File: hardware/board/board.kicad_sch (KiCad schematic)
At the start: 37 parts, among them J101 CM4_UART, J102 CM4_DEBUG, J103 MCU_DEBUG, J104 MCU_UART, J105 Conn_01x01, J106 CM4_STATUS, J107 Barrel_Jack, J108 Conn_01x01, J109 Conn_01x01, J110 Conn_01x01, J111 Conn_01x01, U101 Oled, U104 74LVC1G07SE-7, U105 NCP1117-3.3_SOT223

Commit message: footprints
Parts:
- D101, D102: footprint LED_SMD:LED_0603_1608Metric -> LED_SMD:LED_0805_2012Metric
- J104, J106: footprint (none) -> Connector_PinSocket_2.54mm:PinSocket_1x03_P2.54mm_Vertical
- J105: value Conn_01x01 -> MCU_RUN; footprint (none) -> Connector_PinSocket_2.54mm:PinSocket_1x01_P2.54mm_Vertical
- J107: value Barrel_Jack -> Barrel_5V; footprint (none) -> ledaw:DC-005-5A-2.0
- J108: value Conn_01x01 -> TP_3V3; footprint (none) -> Connector_PinSocket_2.54mm:PinSocket_1x01_P2.54mm_Vertical
- J109: value Conn_01x01 -> TP_1V8; footprint (none) -> Connector_PinSocket_2.54mm:PinSocket_1x01_P2.54mm_Vertical
- J110: value Conn_01x01 -> TP_5V; footprint (none) -> Connector_PinSocket_2.54mm:PinSocket_1x01_P2.54mm_Vertical
- J111: value Conn_01x01 -> TP_GND; footprint (none) -> Connector_PinSocket_2.54mm:PinSocket_1x01_P2.54mm_Vertical
- R101, R102: footprint Resistor_SMD:R_0603_1608Metric_Pad0.98x0.95mm_HandSolder -> Resistor_SMD:R_0805_2012Metric
- TP101, TP102, TP103, TP104, TP105, TP106: footprint (none) -> TestPoint:TestPoint_Keystone_5015_Micro_Mini
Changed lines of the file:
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@@
 		(in_pos_files yes)
 		(dnp no)
-		(fields_autoplaced yes)
 		(property "Reference" "J109"
-			(at 279.4 29.2099 90)
+			(at 274.32 33.528 90)
 			(show_name no)
 			(do_not_autoplace no)
@@
 			)
 		)
-		(property "Value" "Conn_01x01"
-			(at 279.4 31.7499 90)
-			(hide yes)
+		(property "Value" "TP_1V8"
+			(at 274.32 36.068 90)
 			(show_name no)
 			(do_not_autoplace no)
@@
 			)
 		)
-		(property "Footprint" ""
+		(property "Footprint" "Connector_PinSocket_2.54mm:PinSocket_1x01_P2.54mm_Vertical"
 			(at 276.86 30.48 0)
 			(hide yes)
@@
 			)
 		)
-		(property "Value" "Barrel_Jack"
+		(property "Value" "Barrel_5V"
 			(at 226.06 20.32 0)
 			(show_name no)
@@
 			)
 		)
-		(property "Footprint" ""
+		(property "Footprint" "ledaw:DC-005-5A-2.0"
 			(at 227.33 27.686 0)
 			(hide yes)
@@
 			)
 		)
-		(property "Footprint" ""
+		(property "Footprint" "Connector_PinSocket_2.54mm:PinSocket_1x03_P2.54mm_Vertical"
 			(at 274.32 143.51 0)
 			(hide yes)
@@
 			)
 		)
-		(property "Footprint" ""
+		(property "Footprint" "TestPoint:TestPoint_Keystone_5015_Micro_Mini"
 			(at 171.45 236.22 0)
 			(hide yes)
@@
 			)
 		)
-		(property "Footprint" "LED_SMD:LED_0603_1608Metric"
+		(property "Footprint" "LED_SMD:LED_0805_2012Metric"
 			(at 328.93 34.29 0)
 			(hide yes)
@@
 			)
 		)
-		(property "Footprint" ""
+		(property "Footprint" "TestPoint:TestPoint_Keystone_5015_Micro_Mini"
 			(at 243.84 143.51 0)
 			(hide yes)
@@
 			)
 		)
-		(property "Footprint" ""
+		(property "Footprint" "TestPoint:TestPoint_Keystone_5015_Micro_Mini"
 			(at 205.74 236.22 0)
 			(hide yes)
@@
 			)
 		)
-		(property "Value" "Conn_01x01"
+		(property "Value" "TP_GND"
 			(at 288.29 17.7801 90)
-			(hide yes)
 			(show_name no)
 			(do_not_autoplace no)
@@
 			)
 		)
-		(property "Footprint" ""
+		(property "Footprint" "Connector_PinSocket_2.54mm:PinSocket_1x01_P2.54mm_Vertical"
 			(at 285.75 19.05 0)
 			(hide yes)
@@
 			)
 		)
-		(property "Footprint" "Resistor_SMD:R_0603_1608Metric_Pad0.98x0.95mm_HandSolder"
+		(property "Footprint" "Resistor_SMD:R_0805_2012Metric"
 			(at 327.152 46.99 90)
 			(hide yes)
@@
 			)
 		)
-		(property "Footprint" "LED_SMD:LED_0603_1608Metric"
+		(property "Footprint" "LED_SMD:LED_0805_2012Metric"
 			(at 368.3 29.21 0)
 			(hide yes)
@@
 		(in_pos_files yes)
 		(dnp no)
-		(fields_autoplaced yes)
 		(property "Reference" "J110"
-			(at 259.08 29.2099 90)
+			(at 253.492 33.528 90)
 			(show_name no)
 			(do_not_autoplace no)
@@
 			)
 		)
-		(property "Value" "Conn_01x01"
-			(at 259.08 31.7499 90)
-			(hide yes)
+		(property "Value" "TP_5V"
+			(at 253.492 36.068 90)
 			(show_name no)
 			(do_not_autoplace no)
@@
 			)
 		)
-		(property "Footprint" ""
+		(property "Footprint" "Connector_PinSocket_2.54mm:PinSocket_1x01_P2.54mm_Vertical"
 			(at 256.54 30.48 0)
 			(hide yes)
@@
 			)
 		)
-		(property "Value" "Conn_01x01"
+		(property "Value" "MCU_RUN"
 			(at 264.16 165.1 0)
 			(show_name no)
@@
 			)
 		)
-		(property "Footprint" ""
+		(property "Footprint" "Connector_PinSocket_2.54mm:PinSocket_1x01_P2.54mm_Vertical"
 			(at 264.16 161.29 0)
 			(hide yes)
@@
 			)
 		)
-		(property "Footprint" ""
+		(property "Footprint" "Connector_PinSocket_2.54mm:PinSocket_1x03_P2.54mm_Vertical"
 			(at 227.33 184.15 0)
 			(hide yes)
@@
 			)
 		)
-		(property "Footprint" "Resistor_SMD:R_0603_1608Metric_Pad0.98x0.95mm_HandSolder"
+		(property "Footprint" "Resistor_SMD:R_0805_2012Metric"
 			(at 366.522 38.1 90)
 			(hide yes)
@@
 		(in_pos_files yes)
 		(dnp no)
-		(fields_autoplaced yes)
 		(property "Reference" "J108"
-			(at 269.24 29.2099 90)
+			(at 264.16 33.528 90)
 			(show_name no)
 			(do_not_autoplace no)
@@
 			)
 		)
-		(property "Value" "Conn_01x01"
-			(at 269.24 31.7499 90)
-			(hide yes)
+		(property "Value" "TP_3V3"
+			(at 264.16 36.068 90)
 			(show_name no)
 			(do_not_autoplace no)
@@
 			)
 		)
-		(property "Footprint" ""
+		(property "Footprint" "Connector_PinSocket_2.54mm:PinSocket_1x01_P2.54mm_Vertical"
 			(at 266.7 30.48 0)
 			(hide yes)
@@
 			)
 		)
-		(property "Footprint" ""
+		(property "Footprint" "TestPoint:TestPoint_Keystone_5015_Micro_Mini"
 			(at 132.08 148.59 0)
 			(hide yes)
@@
 			)
 		)
-		(property "Footprint" ""
+		(property "Footprint" "TestPoint:TestPoint_Keystone_5015_Micro_Mini"
 			(at 132.08 156.21 0)
 			(hide yes)
@@
 			)
 		)
-		(property "Footprint" ""
+		(property "Footprint" "TestPoint:TestPoint_Keystone_5015_Micro_Mini"
 			(at 307.34 53.34 0)
 			(hide yes)

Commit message: barrel LSCS
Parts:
- J107: LCSC (none) -> C381116
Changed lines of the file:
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@@
+			)
+		)
+		(property "LCSC" "C381116"
+			(at 226.06 26.67 0)
+			(hide yes)
+			(show_name no)
+			(do_not_autoplace no)
+			(effects
+				(font
+					(size 1.27 1.27)
+				)
 			)
 		)

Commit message: lot of testpoints
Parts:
- removed J108: TP_3V3, Connector_PinSocket_2.54mm:PinSocket_1x01_P2.54mm_Vertical, symbol Connector_Generic:Conn_01x01
- removed J109: TP_1V8, Connector_PinSocket_2.54mm:PinSocket_1x01_P2.54mm_Vertical, symbol Connector_Generic:Conn_01x01
- removed J110: TP_5V, Connector_PinSocket_2.54mm:PinSocket_1x01_P2.54mm_Vertical, symbol Connector_Generic:Conn_01x01
- removed J111: TP_GND, Connector_PinSocket_2.54mm:PinSocket_1x01_P2.54mm_Vertical, symbol Connector_Generic:Conn_01x01
- R103, R104: footprint Resistor_SMD:R_0603_1608Metric_Pad0.98x0.95mm_HandSolder -> Resistor_SMD:R_0805_2012Metric
- TP101, TP102, TP103: footprint TestPoint:TestPoint_Keystone_5015_Micro_Mini -> ledaw:named_TestPoint
- TP104: value MCU_3V3_OUTPUT -> CM4_3V3OUT; footprint TestPoint:TestPoint_Keystone_5015_Micro_Mini -> ledaw:named_TestPoint
- TP105: value MCU_1V8_OUTPUT -> CM4_1V8OUT; footprint TestPoint:TestPoint_Keystone_5015_Micro_Mini -> ledaw:named_TestPoint
- TP106: value nLED_ACTIVITY -> GND; footprint TestPoint:TestPoint_Keystone_5015_Micro_Mini -> ledaw:named_TestPoint
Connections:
- net GND: now also TP106.1
- net nLED_Activity: no longer TP106.1

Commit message: more TP and dummy hirose
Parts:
- removed J105: MCU_RUN, Connector_PinSocket_2.54mm:PinSocket_1x01_P2.54mm_Vertical, symbol Connector_Generic:Conn_01x01
- added TP107: GND, ledaw:named_TestPoint, symbol Connector:TestPoint
- J101, J102, J103, J104, J106: footprint Connector_PinSocket_2.54mm:PinSocket_1x03_P2.54mm_Vertical -> ledaw:named_PinSocket_01x03
- U102, U103: footprint Connector_Hirose_DF40:Hirose_DF40C-100DS-0.4V_2x50_P0.4mm -> ledaw:dummy_hirose
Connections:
- net +3V3: now also JP103.2 (B); no longer JP103.1 (A)
- net RUN: now also JP103.1 (A), TP107.1; no longer JP103.2 (B)
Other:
- moved on the sheet: JP103
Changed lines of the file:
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@@
 	)
 	(junction
+		(at 269.24 154.94)
+		(diameter 0)
+		(color 0 0 0 0)
+	)
+	(junction
 		(at 189.23 74.93)
 		(diameter 0)
@@
 	)
 	(junction
-		(at 269.24 154.94)
-		(diameter 0)
-		(color 0 0 0 0)
-	)
-	(junction
 		(at 106.045 71.12)
 		(diameter 0)
@@
 			)
 		)
-		(property "Footprint" "Connector_PinSocket_2.54mm:PinSocket_1x03_P2.54mm_Vertical"
+		(property "Footprint" "ledaw:named_PinSocket_01x03"
 			(at 364.49 83.82 0)
 			(hide yes)
@@
 	(symbol
 		(lib_id "Jumper:Jumper_2_Open")
-		(at 264.16 154.94 0)
+		(at 264.16 154.94 180)
 		(unit 1)
 		(body_style 1)
@@
 		(dnp no)
 		(property "Reference" "JP103"
-			(at 264.16 152.146 0)
+			(at 264.16 157.734 0)
 			(show_name no)
 			(do_not_autoplace no)
@@
 		)
 		(property "Value" "Jumper_SWCLK_Open"
-			(at 264.16 147.828 0)
+			(at 264.16 162.052 0)
 			(hide yes)
 			(show_name no)
@@
 			)
 		)
-		(property "Footprint" "Connector_PinSocket_2.54mm:PinSocket_1x03_P2.54mm_Vertical"
+		(property "Footprint" "ledaw:named_PinSocket_01x03"
 			(at 274.32 143.51 0)
 			(hide yes)
@@
 			)
 		)
-		(property "Footprint" "Connector_Hirose_DF40:Hirose_DF40C-100DS-0.4V_2x50_P0.4mm"
+		(property "Footprint" "ledaw:dummy_hirose"
 			(at 187.96 198.12 0)
 			(hide yes)
@@
 	)
 	(symbol
-		(lib_id "Connector_Generic:Conn_01x01")
-		(at 264.16 161.29 0)
-		(mirror y)
-		(unit 1)
-		(body_style 1)
-		(exclude_from_sim no)
-		(in_bom yes)
-		(on_board yes)
-		(in_pos_files yes)
-		(dnp no)
-		(property "Reference" "J105"
-			(at 264.16 167.64 0)
-			(show_name no)
-			(do_not_autoplace no)
-			(effects
-				(font
-					(size 1.27 1.27)
-				)
-			)
-		)
-		(property "Value" "MCU_RUN"
-			(at 264.16 165.1 0)
-			(show_name no)
-			(do_not_autoplace no)
-			(effects
-				(font
-					(size 1.27 1.27)
-				)
-			)
-		)
-		(property "Footprint" "Connector_PinSocket_2.54mm:PinSocket_1x01_P2.54mm_Vertical"
-			(at 264.16 161.29 0)
-			(hide yes)
-			(show_name no)
-			(do_not_autoplace no)
-			(effects
-				(font
-					(size 1.27 1.27)
-				)
-			)
-		)
-		(property "Datasheet" ""
-			(at 264.16 161.29 0)
-			(hide yes)
-			(show_name no)
-			(do_not_autoplace no)
-			(effects
-				(font
-					(size 1.27 1.27)
-				)
-			)
-		)
-		(property "Description" "Generic connector, single row, 01x01, script generated (kicad-library-utils/schlib/autogen/connector/)"
-			(at 264.16 161.29 0)
-			(hide yes)
-			(show_name no)
-			(do_not_autoplace no)
-			(effects
-				(font
-					(size 1.27 1.27)
-				)
-			)
-		)
-		(pin "1"
-		)
-		(instances
-			(project "board"
-				(path "/dd13fd41-39ab-4435-9074-5024f1786746"
-					(reference "J105")
-					(unit 1)
-				)
-			)
-		)
-	)
-	(symbol
 		(lib_id "Device:C")
 		(at 170.18 241.3 0)
@@
 			)
 		)
-		(property "Footprint" "Connector_PinSocket_2.54mm:PinSocket_1x03_P2.54mm_Vertical"
+		(property "Footprint" "ledaw:named_PinSocket_01x03"
 			(at 227.33 184.15 0)
 			(hide yes)
@@
 	)
 	(symbol
+		(lib_id "Connector:TestPoint")
+		(at 269.24 161.29 180)
+		(unit 1)
+		(body_style 1)
+		(exclude_from_sim no)
+		(in_bom yes)
+		(on_board yes)
+		(in_pos_files yes)
+		(dnp no)
+		(fields_autoplaced yes)
+		(property "Reference" "TP107"
+			(at 271.78 163.3219 0)
+			(show_name no)
+			(do_not_autoplace no)
+			(effects
+				(font
+					(size 1.27 1.27)
+				)
+				(justify right)
+			)
+		)
+		(property "Value" "GND"
+			(at 271.78 165.8619 0)
+			(show_name no)
+			(do_not_autoplace no)
+			(effects
+				(font
+					(size 1.27 1.27)
+				)
+				(justify right)
+			)
+		)
+		(property "Footprint" "ledaw:named_TestPoint"
+			(at 264.16 161.29 0)
+			(hide yes)
+			(show_name no)
+			(do_not_autoplace no)
+			(effects
+				(font
+					(size 1.27 1.27)
+				)
+			)
+		)
+		(property "Datasheet" ""
+			(at 264.16 161.29 0)
+			(hide yes)
+			(show_name no)
+			(do_not_autoplace no)
+			(effects
+				(font
+					(size 1.27 1.27)
+				)
+			)
+		)
+		(property "Description" "test point"
+			(at 269.24 161.29 0)
+			(hide yes)
+			(show_name no)
+			(do_not_autoplace no)
+			(effects
+				(font
+					(size 1.27 1.27)
+				)
+			)
+		)
+		(pin "1"
+		)
+		(instances
+			(project "board"
+				(path "/dd13fd41-39ab-4435-9074-5024f1786746"
+					(reference "TP107")
+					(unit 1)
+				)
+			)
+		)
+	)
+	(symbol
 		(lib_id "Device:R")
 		(at 368.3 38.1 0)
@@
 			)
 		)
-		(property "Footprint" "Connector_PinSocket_2.54mm:PinSocket_1x03_P2.54mm_Vertical"
+		(property "Footprint" "ledaw:named_PinSocket_01x03"
 			(at 353.06 106.68 0)
 			(hide yes)
@@
 			)
 		)
-		(property "Footprint" "Connector_Hirose_DF40:Hirose_DF40C-100DS-0.4V_2x50_P0.4mm"
+		(property "Footprint" "ledaw:dummy_hirose"
 			(at 67.31 196.85 0)
 			(hide yes)
@@
 			)
 		)
-		(property "Footprint" "Connector_PinSocket_2.54mm:PinSocket_1x03_P2.54mm_Vertical"
+		(property "Footprint" "ledaw:named_PinSocket_01x03"
 			(at 373.38 106.68 0)
 			(hide yes)

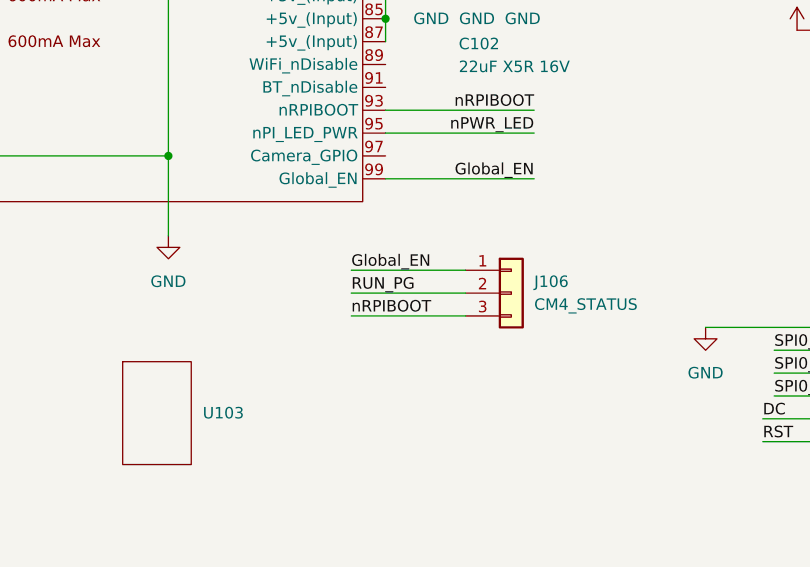
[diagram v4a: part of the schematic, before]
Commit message: fix the dummy hirose and some more TP and Pinsocket
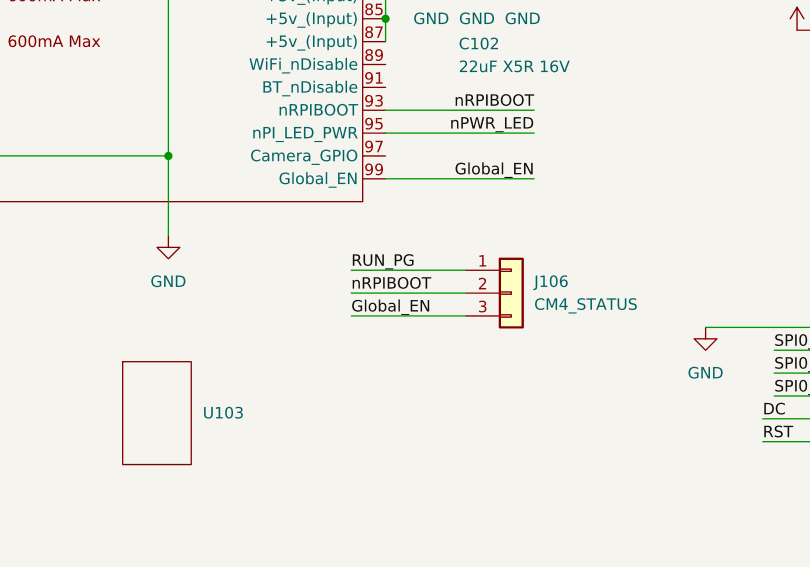
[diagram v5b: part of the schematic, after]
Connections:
- net Global_EN: now also J106.3 (Pin_3); no longer J106.1 (Pin_1)
- net RUN_PG: now also J106.1 (Pin_1); no longer J106.2 (Pin_2)
- net nRPIBOOT: now also J106.2 (Pin_2); no longer J106.3 (Pin_3)

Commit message: add back efuse
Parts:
- added R105: 10k, Resistor_SMD:R_0805_2012Metric, symbol Device:R
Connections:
- net +3V3: now also R105.1; no longer JP103.2 (B)
- new net: JP103.2 (B), R105.2
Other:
- sheet mcu ports: added FUSE_ILM; removed none
- sheet usb ports: added FUSE_ILM; removed none

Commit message: efuse pcb
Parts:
- removed J107: Barrel_5V, ledaw:DC-005-5A-2.0, symbol Connector:Barrel_Jack
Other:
- note removed: "Big test points"

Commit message: DRC
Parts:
- TP101: value LDO_IN -> LDO_IN(5V)
- TP102: value LDO_OUT -> LDO_OUT(3V3)
- TP107: value GND -> RUN
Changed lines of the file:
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@@
 			)
 		)
-		(property "Value" "LDO_IN"
+		(property "Value" "LDO_IN(5V)"
 			(at 168.91 234.1879 0)
 			(show_name no)
@@
 			)
 		)
-		(property "Value" "LDO_OUT"
+		(property "Value" "LDO_OUT(3V3)"
 			(at 203.2 234.1879 0)
 			(show_name no)
@@
 			)
 		)
-		(property "Value" "GND"
+		(property "Value" "RUN"
 			(at 271.78 165.8619 0)
 			(show_name no)
